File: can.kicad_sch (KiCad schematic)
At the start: 19 parts, among them J401 CAN, J402 CAN, SW401 Term, U401 TJA1042T

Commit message: Revisit 3D models
Signed-off-by: Benedikt Spranger <b.spranger@linutronix.de>
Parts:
- D401, D402: footprint LED_SMD:LED_Kingbright_AAA3528ESGCT -> fixes:LED_Kingbright_AAA3528ESGCT
- J402: footprint TerminalBlock_WAGO:TerminalBlock_WAGO_236-402_1x02_P5.00mm_45Degree -> fixes:TerminalBlock_WAGO_236-402_1x02_P5.00mm_45Degree
- SW401: footprint Button_Switch_THT:SW_Push_2P2T_Toggle_CK_PVA2xxH1xxxxxxV2 -> fixes:SW_Push_2P2T_Toggle_CK_PVA2xxH1xxxxxxV2
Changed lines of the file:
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@@
 			)
 		)
-		(property "Footprint" "Button_Switch_THT:SW_Push_2P2T_Toggle_CK_PVA2xxH1xxxxxxV2"
+		(property "Footprint" "fixes:SW_Push_2P2T_Toggle_CK_PVA2xxH1xxxxxxV2"
 			(at 147.32 96.52 0)
 			(effects
@@
 			)
 		)
-		(property "Footprint" "TerminalBlock_WAGO:TerminalBlock_WAGO_236-402_1x02_P5.00mm_45Degree"
+		(property "Footprint" "fixes:TerminalBlock_WAGO_236-402_1x02_P5.00mm_45Degree"
 			(at 132.08 92.71 0)
 			(effects
@@
 			)
 		)
-		(property "Footprint" "LED_SMD:LED_Kingbright_AAA3528ESGCT"
+		(property "Footprint" "fixes:LED_Kingbright_AAA3528ESGCT"
 			(at 78.74 46.482 0)
 			(effects
@@
 			)
 		)
-		(property "Footprint" "LED_SMD:LED_Kingbright_AAA3528ESGCT"
+		(property "Footprint" "fixes:LED_Kingbright_AAA3528ESGCT"
 			(at 53.34 46.482 0)
 			(effects

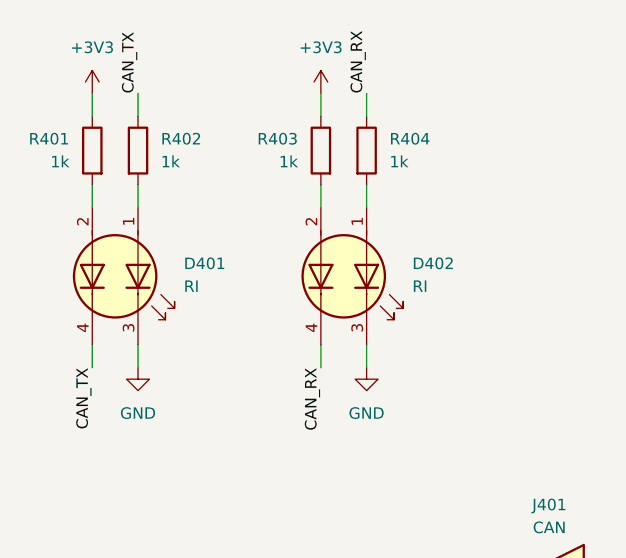
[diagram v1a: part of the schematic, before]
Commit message: Fix Dual LED footprint issue
Signed-off-by: Benedikt Spranger <b.spranger@linutronix.de>
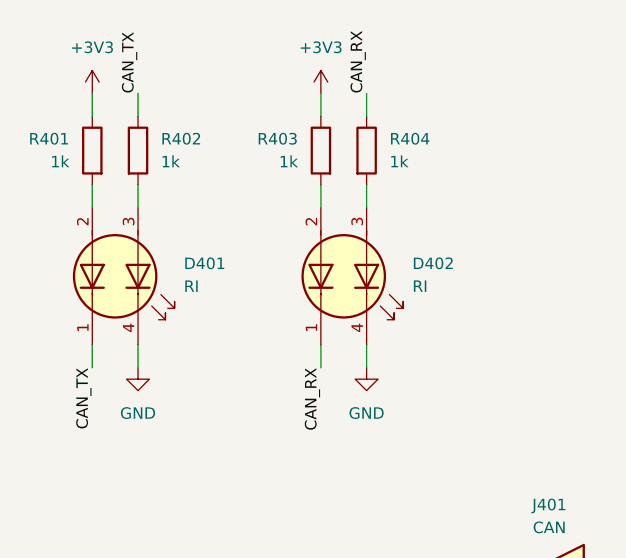
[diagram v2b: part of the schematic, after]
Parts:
- D401, D402: symbol Device:LED_Dual_AAKK -> led:LED_Dual_KAAK
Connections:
- net CAN_RX: now also D402.1 (K2); no longer D402.4 (K2)
- net CAN_TX: now also D401.1 (K2); no longer D401.4 (K2)
- net GND: now also D401.4 (K1), D402.4 (K1); no longer D401.3 (K1), D402.3 (K1)
- net at R404.2: now also D402.3 (A1); no longer D402.1 (A1)
- net at R402.2: now also D401.3 (A1); no longer D401.1 (A1)
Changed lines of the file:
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@@
 	)
 	(symbol
-		(lib_id "Device:LED_Dual_AAKK")
+		(lib_id "led:LED_Dual_KAAK")
 		(at 78.74 45.72 270)
 		(unit 1)
@@
 			)
 		)
-		(property "Description" "Dual LED, cathodes on pins 3 and 4"
+		(property "Description" "Dual LED, cathodes on pins 1 and 4"
 			(at 78.74 45.72 0)
 			(effects
@@
 	)
 	(symbol
-		(lib_id "Device:LED_Dual_AAKK")
+		(lib_id "led:LED_Dual_KAAK")
 		(at 53.34 45.72 270)
 		(unit 1)
@@
 			)
 		)
-		(property "Description" "Dual LED, cathodes on pins 3 and 4"
+		(property "Description" "Dual LED, cathodes on pins 1 and 4"
 			(at 53.34 45.72 0)
 			(effects
@@
 			(effects
 				(font
+					(size 1.27 1.27)
+				)
+				(hide yes)
+			)
+		)
+		(property "digikey#" ""
+			(at 53.34 45.72 0)
+			(effects
+				(font
+					(size 1.27 1.27)
+				)
+				(hide yes)
+			)
+		)
+		(property "tme#" ""
+			(at 53.34 45.72 0)
+			(effects
+				(font

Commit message: Add USB termination resistors
Signed-off-by: Benedikt Spranger <b.spranger@linutronix.de>
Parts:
- renumbered JP403 to JP401, JP401 to JP402, JP402 to JP403, R406 to R405, R408 to R406, R405 to R407, R407 to R408
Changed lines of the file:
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@@
 		(on_board yes)
 		(dnp no)
-		(property "Reference" "R407"
+		(property "Reference" "R408"
 			(at 214.63 93.98 90)
 			(effects
@@
 			(project "sertest-ng"
 				(path "/9a3cad5d-0a7b-485e-a592-d3e508a0fc7b/1741690d-1b44-488b-a373-15edd4d8ea4f"
-					(reference "R407")
+					(reference "R408")
 					(unit 1)
 				)
@@
 		(on_board yes)
 		(dnp no)
-		(property "Reference" "JP403"
+		(property "Reference" "JP401"
 			(at 115.57 105.4099 90)
 			(effects
@@
 			(project ""
 				(path "/9a3cad5d-0a7b-485e-a592-d3e508a0fc7b/1741690d-1b44-488b-a373-15edd4d8ea4f"
-					(reference "JP403")
+					(reference "JP401")
 					(unit 1)
 				)
@@
 		(dnp no)
 		(fields_autoplaced yes)
-		(property "Reference" "R408"
+		(property "Reference" "R406"
 			(at 172.72 96.5199 0)
 			(effects
@@
 			(project "sertest-ng"
 				(path "/9a3cad5d-0a7b-485e-a592-d3e508a0fc7b/1741690d-1b44-488b-a373-15edd4d8ea4f"
-					(reference "R408")
+					(reference "R406")
 					(unit 1)
 				)
@@
 		(dnp no)
 		(fields_autoplaced yes)
-		(property "Reference" "JP402"
+		(property "Reference" "JP403"
 			(at 228.6 101.6 0)
 			(effects
@@
 			(project "sertest-ng"
 				(path "/9a3cad5d-0a7b-485e-a592-d3e508a0fc7b/1741690d-1b44-488b-a373-15edd4d8ea4f"
-					(reference "JP402")
+					(reference "JP403")
 					(unit 1)
 				)
@@
 		(dnp no)
 		(fields_autoplaced yes)
-		(property "Reference" "R406"
+		(property "Reference" "R405"
 			(at 172.72 83.8199 0)
 			(effects
@@
 			(project "sertest-ng"
 				(path "/9a3cad5d-0a7b-485e-a592-d3e508a0fc7b/1741690d-1b44-488b-a373-15edd4d8ea4f"
-					(reference "R406")
+					(reference "R405")
 					(unit 1)
 				)
@@
 		(dnp no)
 		(fields_autoplaced yes)
-		(property "Reference" "JP401"
+		(property "Reference" "JP402"
 			(at 228.6 71.12 0)
 			(effects
@@
 			(project ""
 				(path "/9a3cad5d-0a7b-485e-a592-d3e508a0fc7b/1741690d-1b44-488b-a373-15edd4d8ea4f"
-					(reference "JP401")
+					(reference "JP402")
 					(unit 1)
 				)
@@
 		(on_board yes)
 		(dnp no)
-		(property "Reference" "R405"
+		(property "Reference" "R407"
 			(at 214.63 81.534 90)
 			(effects
@@
 			(project "sertest-ng"
 				(path "/9a3cad5d-0a7b-485e-a592-d3e508a0fc7b/1741690d-1b44-488b-a373-15edd4d8ea4f"
-					(reference "R405")
-					(unit 1)
-				)
+					(reference "R407")
+					(unit 1)
+				)
